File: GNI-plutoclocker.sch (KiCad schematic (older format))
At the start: 65 parts, among them J1 PLUTO_RF_IN, J2 PLUTO_5V, J3 PLUTO_40MHZ_IN, J4 10MHZ_IN, J5 LNB_OUT, J6 10MHZ_OUT, J7 I2C_PROG, J8 18V_ENA, U1 MIC5504-3.3YM5, U2 MIC5504-1.8YM5, U3 TPS61085, U4 CDCE913

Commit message: adding some project changes and fab outputs
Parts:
- removed C20: 10p, Capacitor_SMD:C_0805_2012Metric, symbol Device:C_Small
- removed C6: 10u, Capacitor_THT:CP_Radial_D8.0mm_P3.80mm, symbol Device:C_Polarized_Small
- removed J7: I2C_PROG, Connector_PinSocket_2.54mm:PinSocket_1x04_P2.54mm_Vertical, symbol Connector_Generic:Conn_01x04
- added C12, C6: 10u, Capacitor_SMD:C_0805_2012Metric, symbol Device:C_Small
- added J7: I2C_PROG, Connector_PinSocket_2.54mm:PinSocket_1x03_P2.54mm_Vertical, symbol Connector_Generic:Conn_01x03
- added L9: 4.7uH, Inductor_SMD:L_0805_2012Metric_Pad1.15x1.40mm_HandSolder, symbol Device:L
- added TP1: S0_PAD, Connector_PinSocket_2.54mm:PinSocket_1x01_P2.54mm_Vertical, symbol Connector:TestPoint
- C10, C9: value 1n -> 100n
- J8: footprint Inductor_SMD:L_0805_2012Metric_Pad1.15x1.40mm_HandSolder -> TestPoint:TestPoint_2Pads_Pitch2.54mm_Drill0.8mm
- L3: footprint Inductor_SMD:L_0805_2012Metric_Pad1.15x1.40mm_HandSolder -> Inductor_SMD:L_Fastron_PISN_Handsoldering
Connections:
- net +5V: now also C6.1, L9.2; no longer C2.1, C3.1, U1.1 (VIN), U1.3 (EN), U2.1 (VIN), U2.3 (EN)
- net GND: now also C12.2, C6.2, J7.3 (Pin_3)
- net at R17.2, U4.12 (S2/SCL): now also J7.2 (Pin_2)
- net at R16.2, U4.13 (S1/SDA): now also J7.1 (Pin_1)
- net at U4.2 (S0): now also TP1.1
- new net: C12.1, C2.1, C3.1, L9.1, U1.1 (VIN), U1.3 (EN), U2.1 (VIN), U2.3 (EN)
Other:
- moved on the sheet: C10, C16, C17, C2, C3, C9, R16, R17, U1, U2

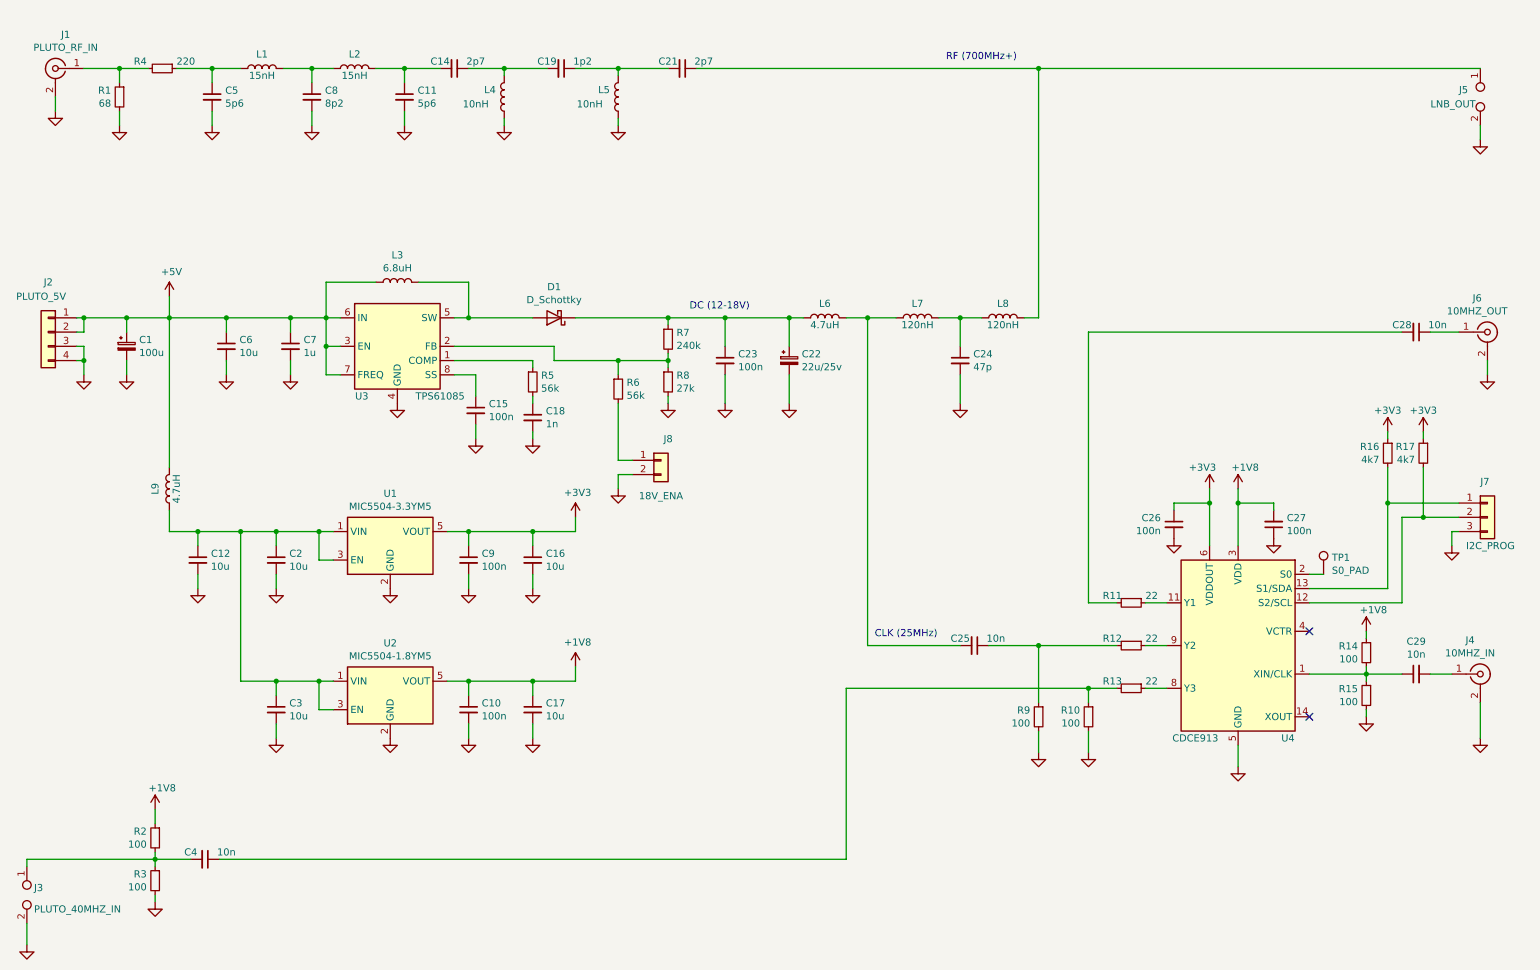
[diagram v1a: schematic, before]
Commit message: minor aesthetics schematics and silk layer adjustments
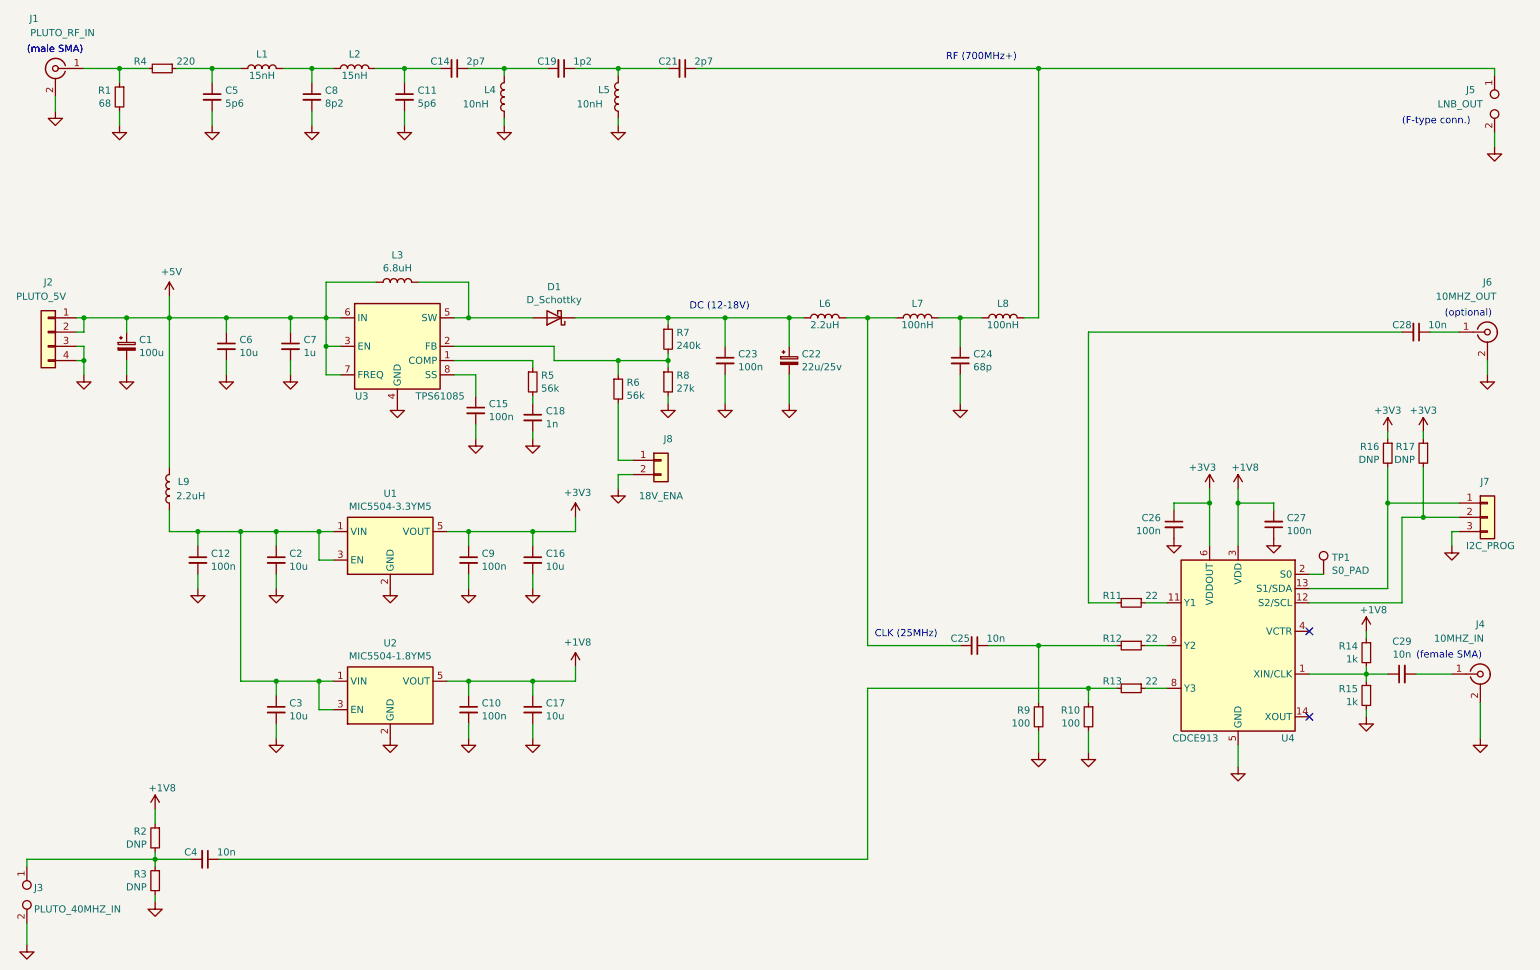
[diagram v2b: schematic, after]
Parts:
- C12: value 10u -> 100n
- C24: value 47p -> 68p
- L6, L9: value 4.7uH -> 2.2uH
- L7, L8: value 120nH -> 100nH
- R14, R15: value 100 -> 1k
- R16, R17: value 4k7 -> DNP
- R2, R3: value 100 -> DNP
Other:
- note added: "(F-type conn.)"
- note added: "(female SMA)"
- note added: "(male SMA)"
- note added: "(optional)"
- moved on the sheet: C29, J5
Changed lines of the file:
@@
 P 10500 4050
 F 0 "R17" H 10559 4096 50  0000 L CNN
-F 1 "4k7" H 10559 4005 50  0000 L CNN
+F 1 "DNP" H 10559 4005 50  0000 L CNN
 F 2 "Resistor_SMD:R_0805_2012Metric" H 10500 4050 50  0001 C CNN
 F 3 "~" H 10500 4050 50  0001 C CNN
@@
 P 10250 4050
 F 0 "R16" H 10309 4096 50  0000 L CNN
-F 1 "4k7" H 10309 4005 50  0000 L CNN
+F 1 "DNP" H 10309 4005 50  0000 L CNN
 F 2 "Resistor_SMD:R_0805_2012Metric" H 10250 4050 50  0001 C CNN
 F 3 "~" H 10250 4050 50  0001 C CNN
@@
 U 1 1 5FB3F2E6
 P 900 1350
-F 0 "J1" H 828 1588 50  0000 C CNN
-F 1 "PLUTO_RF_IN" H 828 1497 50  0000 C CNN
+F 0 "J1" H 1050 1700 50  0000 C CNN
+F 1 "PLUTO_RF_IN" H 850 1600 50  0000 C CNN
 F 2 "Connector_Coaxial:SMA_Samtec_SMA-J-P-X-ST-EM1_EdgeMount" H 900 1350 50  0001 C CNN
 F 3 " ~" H 900 1350 50  0001 C CNN
@@
 L power:GND #PWR049
 U 1 1 5FB4FA9C
-P 10900 1850
-F 0 "#PWR049" H 10900 1600 50  0001 C CNN
-F 1 "GND" H 10905 1677 50  0001 C CNN
-F 2 "" H 10900 1850 50  0001 C CNN
-F 3 "" H 10900 1850 50  0001 C CNN
-	1    10900 1850
-	-1   0    0    -1
-$EndComp
-Wire Wire Line
-	10900 1850 10900 1750
+P 11000 1900
+F 0 "#PWR049" H 11000 1650 50  0001 C CNN
+F 1 "GND" H 11005 1727 50  0001 C CNN
+F 2 "" H 11000 1900 50  0001 C CNN
+F 3 "" H 11000 1900 50  0001 C CNN
+	1    11000 1900
+	-1   0    0    -1
+$EndComp
+Wire Wire Line
+	11000 1900 11000 1800
 $Comp
 L Device:R_Small R2
@@
 P 1600 6750
 F 0 "R2" H 1659 6796 50  0000 L CNN
-F 1 "100" H 1659 6705 50  0000 L CNN
+F 1 "DNP" H 1659 6705 50  0000 L CNN
 F 2 "Resistor_SMD:R_0805_2012Metric" H 1600 6750 50  0001 C CNN
 F 3 "~" H 1600 6750 50  0001 C CNN
@@
 P 1600 7050
 F 0 "R3" H 1659 7096 50  0000 L CNN
-F 1 "100" H 1659 7005 50  0000 L CNN
+F 1 "DNP" H 1659 7005 50  0000 L CNN
 F 2 "Resistor_SMD:R_0805_2012Metric" H 1600 7050 50  0001 C CNN
 F 3 "~" H 1600 7050 50  0001 C CNN
@@
 P 6300 3100
 F 0 "L6" V 6400 3100 50  0000 C CNN
-F 1 "4.7uH" V 6250 3100 50  0000 C CNN
+F 1 "2.2uH" V 6250 3100 50  0000 C CNN
 F 2 "Inductor_SMD:L_0805_2012Metric_Pad1.15x1.40mm_HandSolder" H 6300 3100 50  0001 C CNN
 F 3 "~" H 6300 3100 50  0001 C CNN
@@
 P 6950 3100
 F 0 "L7" V 7050 3100 50  0000 C CNN
-F 1 "120nH" V 6900 3100 50  0000 C CNN
+F 1 "100nH" V 6900 3100 50  0000 C CNN
 F 2 "Inductor_SMD:L_0805_2012Metric_Pad1.15x1.40mm_HandSolder" H 6950 3100 50  0001 C CNN
 F 3 "~" H 6950 3100 50  0001 C CNN
@@
 P 7250 3400
 F 0 "C24" H 7342 3446 50  0000 L CNN
-F 1 "47p" H 7342 3355 50  0000 L CNN
+F 1 "68p" H 7342 3355 50  0000 L CNN
 F 2 "Capacitor_SMD:C_0805_2012Metric" H 7250 3400 50  0001 C CNN
 F 3 "~" H 7250 3400 50  0001 C CNN
@@
 P 7550 3100
 F 0 "L8" V 7650 3100 50  0000 C CNN
-F 1 "120nH" V 7500 3100 50  0000 C CNN
+F 1 "100nH" V 7500 3100 50  0000 C CNN
 F 2 "Inductor_SMD:L_0805_2012Metric_Pad1.15x1.40mm_HandSolder" H 7550 3100 50  0001 C CNN
 F 3 "~" H 7550 3100 50  0001 C CNN
@@
 U 1 1 5FC41AE6
 P 10950 3200
-F 0 "J6" H 10878 3438 50  0000 C CNN
-F 1 "10MHZ_OUT" H 10878 3347 50  0000 C CNN
+F 0 "J6" H 10950 3550 50  0000 C CNN
+F 1 "10MHZ_OUT" H 10800 3450 50  0000 C CNN
 F 2 "Connector_Coaxial:SMA_Samtec_SMA-J-P-X-ST-EM1_EdgeMount" H 10950 3200 50  0001 C CNN
 F 3 " ~" H 10950 3200 50  0001 C CNN
@@
 P 10100 5750
 F 0 "R15" H 10159 5796 50  0000 L CNN
-F 1 "100" H 10159 5705 50  0000 L CNN
+F 1 "1k" H 10159 5705 50  0000 L CNN
 F 2 "Resistor_SMD:R_0805_2012Metric" H 10100 5750 50  0001 C CNN
 F 3 "~" H 10100 5750 50  0001 C CNN
@@
 P 10100 5450
 F 0 "R14" H 10159 5496 50  0000 L CNN
-F 1 "100" H 10159 5405 50  0000 L CNN
+F 1 "1k" H 10159 5405 50  0000 L CNN
 F 2 "Resistor_SMD:R_0805_2012Metric" H 10100 5450 50  0001 C CNN
 F 3 "~" H 10100 5450 50  0001 C CNN
@@
 $EndComp
 Wire Wire Line
-	10350 5600 10100 5600
-Wire Wire Line
-	10700 5600 10550 5600
+	10250 5600 10100 5600
+Wire Wire Line
+	10700 5600 10450 5600
 $Comp
 L Device:C_Small C29
 U 1 1 5FAE5191
-P 10450 5600
-F 0 "C29" V 10221 5600 50  0000 C CNN
-F 1 "10n" V 10312 5600 50  0000 C CNN
-F 2 "Capacitor_SMD:C_0805_2012Metric" H 10450 5600 50  0001 C CNN
-F 3 "~" H 10450 5600 50  0001 C CNN
-	1    10450 5600
+P 10350 5600
+F 0 "C29" V 10121 5600 50  0000 C CNN
+F 1 "10n" V 10212 5600 50  0000 C CNN
+F 2 "Capacitor_SMD:C_0805_2012Metric" H 10350 5600 50  0001 C CNN
+F 3 "~" H 10350 5600 50  0001 C CNN
+	1    10350 5600
 	0    -1   1    0
 $EndComp
@@
 U 1 1 5FADFEA6
 P 10900 5600
-F 0 "J4" H 10828 5838 50  0000 C CNN
-F 1 "10MHZ_IN" H 10828 5747 50  0000 C CNN
+F 0 "J4" H 10900 5950 50  0000 C CNN
+F 1 "10MHZ_IN" H 10750 5850 50  0000 C CNN
 F 2 "Connector_Coaxial:SMA_Samtec_SMA-J-P-X-ST-EM1_EdgeMount" H 10900 5600 50  0001 C CNN
 F 3 " ~" H 10900 5600 50  0001 C CNN
@@
 	8150 3200 10350 3200
 Wire Wire Line
-	2050 6900 6450 6900
-Wire Wire Line
-	6450 6900 6450 5700
-Wire Wire Line
-	6450 5700 8150 5700
+	2050 6900 6600 6900
+Wire Wire Line
+	6600 6900 6600 5700
+Wire Wire Line
+	6600 5700 8150 5700
 Wire Wire Line
 	6600 3100 6600 5400
@@
 L Connector:TestPoint_2Pole J5
 U 1 1 5FC2CC3D
-P 10900 1550
-F 0 "J5" V 10850 1400 50  0000 L CNN
-F 1 "LNB_OUT" V 10950 1200 50  0000 L CNN
-F 2 "TestPoint:TestPoint_2Pads_Pitch2.54mm_Drill0.8mm" H 10900 1550 50  0001 C CNN
-F 3 "~" H 10900 1550 50  0001 C CNN
-	1    10900 1550
-	0    1    1    0
-$EndComp
-Wire Wire Line
-	7800 1350 10900 1350
+P 11000 1600
+F 0 "J5" V 10900 1400 50  0000 L CNN
+F 1 "LNB_OUT" V 11000 1200 50  0000 L CNN
+F 2 "TestPoint:TestPoint_2Pads_Pitch2.54mm_Drill0.8mm" H 11000 1600 50  0001 C CNN
+F 3 "~" H 11000 1600 50  0001 C CNN
+	1    11000 1600
+	0    1    1    0
+$EndComp
 $Comp
 L Connector:TestPoint_2Pole J3
@@
 U 1 1 5FC8ED48
 P 1700 4300
-F 0 "L9" V 1800 4300 50  0000 C CNN
-F 1 "4.7uH" V 1650 4300 50  0000 C CNN
+F 0 "L9" H 1600 4250 50  0000 C CNN
+F 1 "2.2uH" H 1550 4350 50  0000 C CNN
 F 2 "Inductor_SMD:L_0805_2012Metric_Pad1.15x1.40mm_HandSolder" H 1700 4300 50  0001 C CNN
 F 3 "~" H 1700 4300 50  0001 C CNN
@@
 P 1900 4800
 F 0 "C12" H 1992 4846 50  0000 L CNN
-F 1 "10u" H 1992 4755 50  0000 L CNN
+F 1 "100n" H 1992 4755 50  0000 L CNN
 F 2 "Capacitor_SMD:C_0805_2012Metric" H 1900 4800 50  0001 C CNN
 F 3 "~" H 1900 4800 50  0001 C CNN
@@
 Wire Wire Line
 	2200 4600 2450 4600
+Text Notes 700  1250 0    50   ~ 0
+(male SMA)
+Text Notes 700  1250 0    50   ~ 0
+(male SMA)
+Text Notes 10350 1750 0    50   ~ 0
+(F-type conn.)
+Text Notes 10450 5500 0    50   ~ 0
+(female SMA)
+Text Notes 10650 3100 0    50   ~ 0
+(optional)
+Wire Wire Line
+	11000 1350 11000 1400
+Wire Wire Line
+	7800 1350 11000 1350
 $EndSCHEMATC

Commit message: next revision candidate - adding some solderbridge multiplexing options
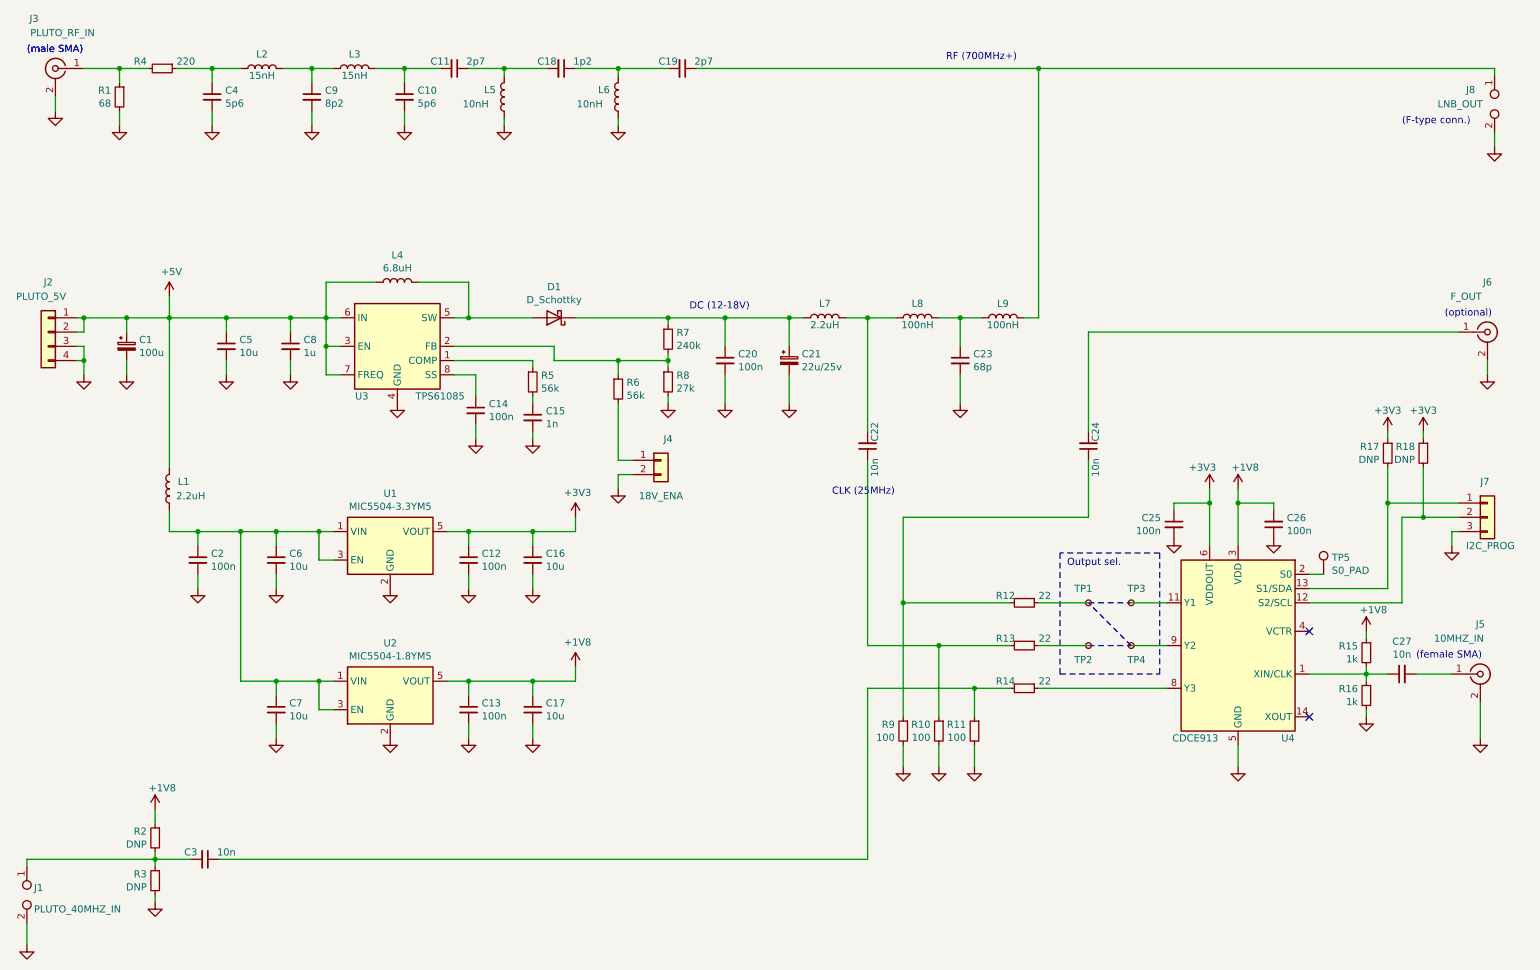
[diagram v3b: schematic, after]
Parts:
- removed C1: 100u, Capacitor_THT:CP_Radial_D8.0mm_P3.80mm, symbol Device:C_Polarized_Small
- removed C22: 22u/25v, Capacitor_THT:CP_Radial_D8.0mm_P3.80mm, symbol Device:C_Polarized_Small
- added C1: 100u, Capacitor_THT:CP_Radial_D8.0mm_P3.80mm, symbol Device:CP_Small
- added C21: 22u/25v, Capacitor_THT:CP_Radial_D8.0mm_P3.80mm, symbol Device:CP_Small
- added R9: 100, Resistor_SMD:R_0805_2012Metric, symbol Device:R_Small
- added TP1, TP2, TP3, TP4: TestPoint_Small, TestPoint:TestPoint_Pad_D1.0mm, symbol Connector:TestPoint_Small
- J6: value 10MHZ_OUT -> F_OUT
- TP5: renamed from TP1; footprint Connector_PinSocket_2.54mm:PinSocket_1x01_P2.54mm_Vertical -> TestPoint:TestPoint_Pad_D1.0mm
- renumbered C11 to C10, C14 to C11, C9 to C12, C10 to C13, C15 to C14, C18 to C15, C19 to C18, C21 to C19, C12 to C2, C23 to C20, C25 to C22, C24 to C23, C28 to C24, C26 to C25, C27 to C26, C29 to C27, C4 to C3, C5 to C4, C6 to C5, C2 to C6, C3 to C7, C7 to C8, C8 to C9, J3 to J1, J1 to J3, J8 to J4, J4 to J5, J5 to J8, L9 to L1, L1 to L2, L2 to L3, L3 to L4, L4 to L5, L5 to L6, L6 to L7, L7 to L8, L8 to L9, R9 to R10, R10 to R11, R11 to R12, R12 to R13, R13 to R14, R14 to R15, R15 to R16, R16 to R17, R17 to R18
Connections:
- net +5V: now also C1.1
- net GND: now also C1.2, C21.2, R9.2
- net at U4.11 (Y1): now also TP3.1; no longer R12.1
- net at U4.9 (Y2): now also TP4.1; no longer R13.1
- net at C20.1, D1.1 (K), L7.1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: now also C21.1
- net at R12.2: now also C24.1, R9.1; no longer C24.2
- net at J6.1 (In): now also C24.2; no longer C24.1
- new net: R12.1, TP1.1
- new net: R13.1, TP2.1
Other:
- note added: "Output sel."
- moved on the sheet: C22, C24, R10, R11, R12, R13, R14
